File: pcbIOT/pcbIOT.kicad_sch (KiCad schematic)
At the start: 30 parts, among them IC1 NRF52832-QFAA-G-R7, IC2 TPS62841DGRR, J1 Battery power in, J2 Conn_01x08_Socket, J3 Conn_01x03_Pin, J4 Conn_01x06_Socket, J5 Conn_01x06_Socket, X1 32MHz

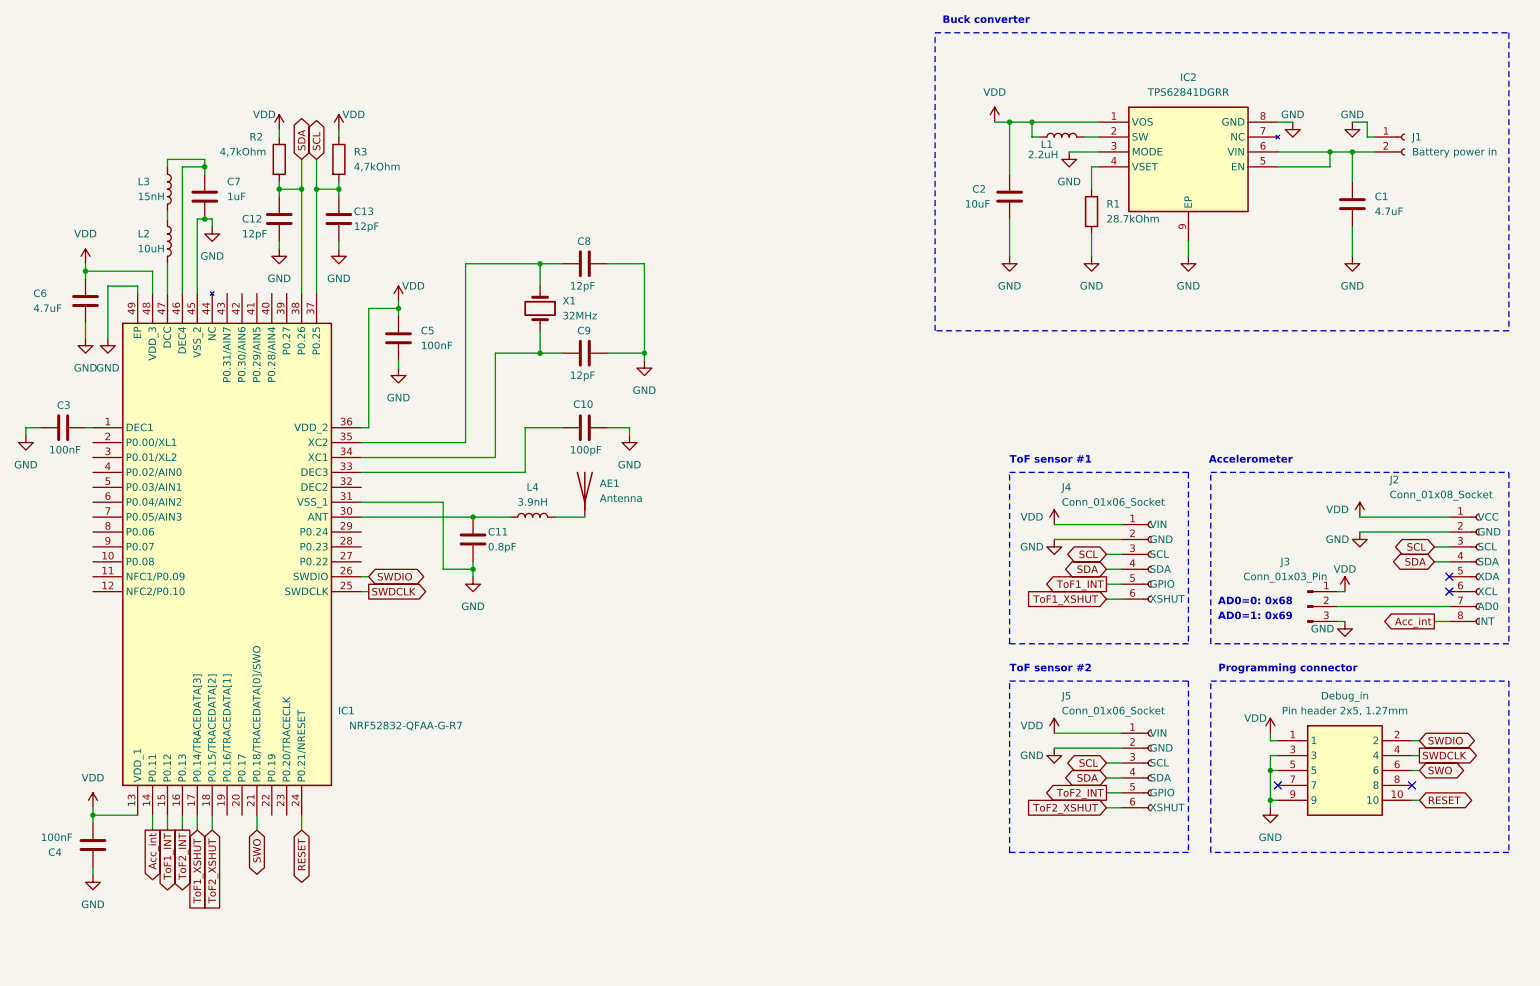
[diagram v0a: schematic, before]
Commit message: Update pcbIOT.kicad_sch
Vervangen buck converter en aanpassing weerstandswaarde naar correcte value
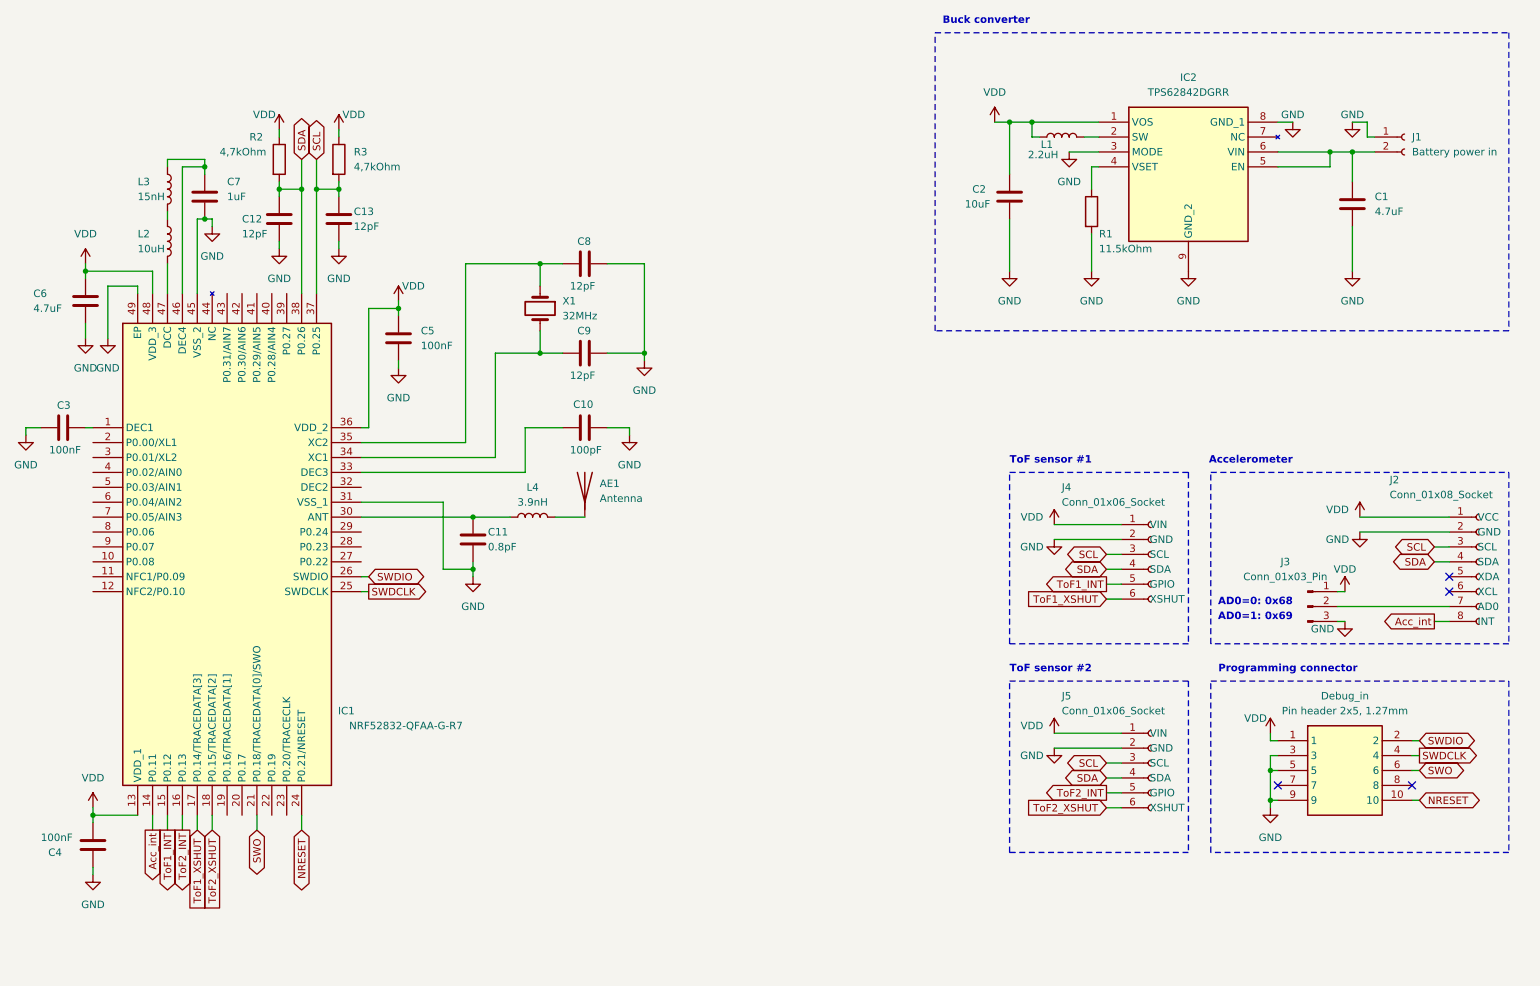
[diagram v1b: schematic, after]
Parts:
- removed IC2: TPS62841DGRR, SOP65P490X110-9N, symbol TPS62841DGRR:TPS62841DGRR
- added IC2: TPS62842DGRR, SOP65P490X110-9N, symbol TPS62842DGRR:TPS62842DGRR
- R1: value 28.7kOhm -> 11.5kOhm
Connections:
- net GND: now also IC2.3 (MODE), IC2.8 (GND_1), IC2.9 (GND_2)
- net VDD: now also IC2.1 (VOS)
- net at L1.2: now also IC2.2 (SW)
- net at R1.1: now also IC2.4 (VSET)
- net at C1.1, J1.2 (Pin_2): now also IC2.5 (EN), IC2.6 (VIN)
- net RESET renamed NRESET

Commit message: Update pcbIOT.kicad_sch
Laatste versie schema + alle footprints ok
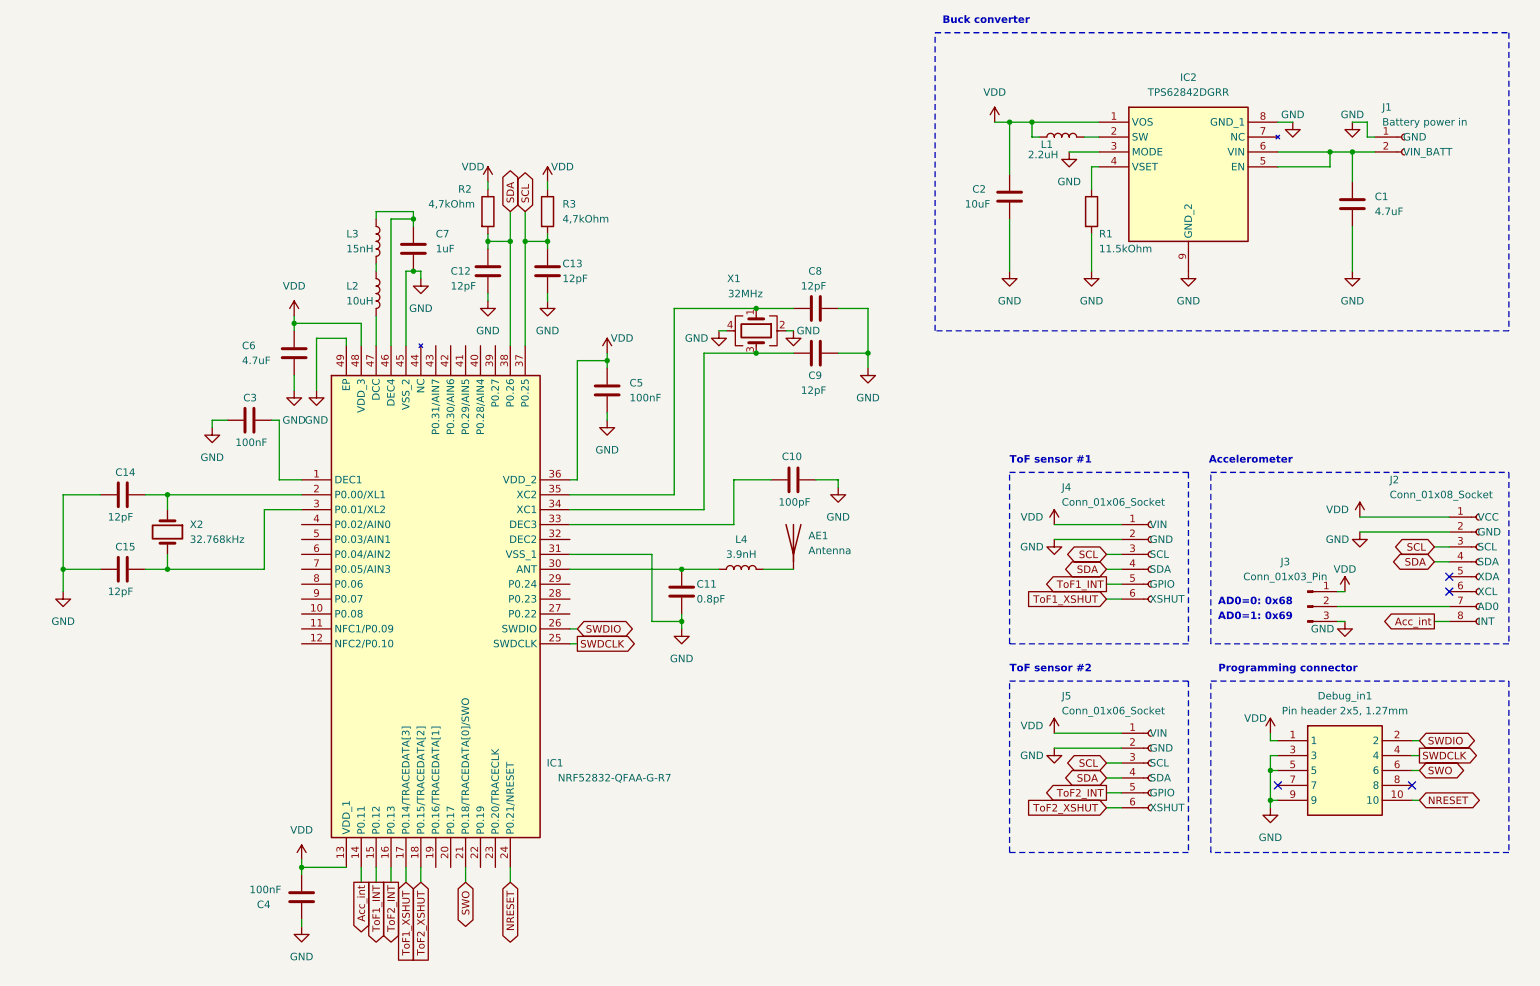
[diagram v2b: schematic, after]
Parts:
- removed X1: 32MHz, symbol Device:Crystal
- added C14, C15: 12pF, Capacitor_SMD:C_0603_1608Metric, symbol Device:C
- added X1: 32MHz, footprints:CX2016DB32000D0FLJCC, symbol Device:Crystal_GND24
- added X2: 32.768kHz, footprints:NX3215SA32768KSTDMUA9, symbol Device:Crystal
- AE1: footprint (none) -> RF_Antenna:Texas_SWRA117D_2.4GHz_Right
- C1, C10, C11, C12, C13, C2, C3, C4, C5, C6, C7, C8, C9: footprint (none) -> Capacitor_SMD:C_0603_1608Metric
- Debug_in1: renamed from Debug_in; footprint FTSH10501LDVK -> footprints:FTSH10501LDVK
- IC1: footprint QFN40P600X600X95-49N -> footprints:QFN40P600X600X95-49N
- IC2: footprint SOP65P490X110-9N -> footprints:SOP65P490X110-9N
- J1: footprint (none) -> Connector_JST:JST_PH_B2B-PH-K_1x02_P2.00mm_Vertical
- J2: footprint (none) -> Connector_PinSocket_2.54mm:PinSocket_1x08_P2.54mm_Vertical
- J3: footprint (none) -> Connector_PinHeader_2.54mm:PinHeader_1x03_P2.54mm_Vertical
- J4, J5: footprint (none) -> Connector_PinSocket_2.54mm:PinSocket_1x06_P2.54mm_Vertical
- L1: footprint (none) -> Inductor_SMD:L_Murata_DFE201610P
- L2: footprint (none) -> Inductor_SMD:L_0603_1608Metric_Pad1.05x0.95mm_HandSolder
- L3: footprint (none) -> footprints:LQW18AS10NG0CD
- L4: footprint (none) -> Inductor_SMD:L_01005_0402Metric_Pad0.57x0.30mm_HandSolder
- R1, R2, R3: footprint (none) -> Resistor_SMD:R_0603_1608Metric
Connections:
- net GND: now also C14.2, C15.2, X1.2, X1.4
- net at C8.2, IC1.35 (XC2): now also X1.1
- net at C9.2, IC1.34 (XC1): now also X1.3
- net at IC1.2 (P0.00/XL1): now also C14.1, X2.1
- net at IC1.3 (P0.01/XL2): now also C15.1, X2.2
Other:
- moved on the sheet: AE1, C10, C11, C12, C13, C3, C4, C5, C6, C7, C8, C9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

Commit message: pcb bijna af
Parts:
- added R4: 1.5kOhm, Resistor_SMD:R_0805_2012Metric_Pad1.20x1.40mm_HandSolder, symbol Device:R
- C1, C10, C11, C12, C13, C14, C15, C2, C3, C4, C5, C6, C7, C8, C9: footprint Capacitor_SMD:C_0603_1608Metric -> Capacitor_SMD:C_0805_2012Metric_Pad1.18x1.45mm_HandSolder
- L4: footprint Inductor_SMD:L_01005_0402Metric_Pad0.57x0.30mm_HandSolder -> Inductor_SMD:L_0805_2012Metric_Pad1.15x1.40mm_HandSolder
- R1: value 11.5kOhm -> 10kOhm; footprint Resistor_SMD:R_0603_1608Metric -> Resistor_SMD:R_0805_2012Metric_Pad1.20x1.40mm_HandSolder
- R2, R3: footprint Resistor_SMD:R_0603_1608Metric -> Resistor_SMD:R_0805_2012Metric_Pad1.20x1.40mm_HandSolder
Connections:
- net GND: now also R4.2; no longer R1.2
- new net: R1.2, R4.1
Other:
- moved on the sheet: R1
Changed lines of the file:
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@@
-    (stroke (width 0) (type default))
-  )
-  (wire (pts (xy 209.55 52.07) (xy 209.55 58.42))
     (stroke (width 0) (type default))
   )
@@
     (stroke (width 0) (type default))
   )
-  (wire (pts (xy 209.55 40.64) (xy 209.55 44.45))
-    (stroke (width 0) (type default))
-  )
   (wire (pts (xy 95.25 58.42) (xy 93.98 58.42))
     (stroke (width 0) (type default))
@@
     (stroke (width 0) (type default))
   )
+  (wire (pts (xy 209.55 49.53) (xy 209.55 50.8))
+    (stroke (width 0) (type default))
+  )
   (wire (pts (xy 212.09 149.86) (xy 214.63 149.86))
     (stroke (width 0) (type default))
@@
   )
   (wire (pts (xy 71.12 93.98) (xy 71.12 83.82))
+    (stroke (width 0) (type default))
+  )
+  (wire (pts (xy 209.55 40.64) (xy 209.55 41.91))
     (stroke (width 0) (type default))
   )
@@
       (effects (font (size 1.27 1.27)) (justify left))
     )
-    (property "Footprint" "Capacitor_SMD:C_0603_1608Metric" (at 74.6252 76.2 0)
+    (property "Footprint" "Capacitor_SMD:C_0805_2012Metric_Pad1.18x1.45mm_HandSolder" (at 74.6252 76.2 0)
       (effects (font (size 1.27 1.27)) hide)
     )
@@
       (effects (font (size 1.27 1.27)) (justify left))
     )
-    (property "Footprint" "Capacitor_SMD:C_0603_1608Metric" (at 158.75 65.7352 0)
+    (property "Footprint" "Capacitor_SMD:C_0805_2012Metric_Pad1.18x1.45mm_HandSolder" (at 158.75 65.7352 0)
       (effects (font (size 1.27 1.27)) hide)
     )
@@
       (effects (font (size 1.27 1.27)) (justify left))
     )
-    (property "Footprint" "Capacitor_SMD:C_0603_1608Metric" (at 40.64 110.1852 0)
+    (property "Footprint" "Capacitor_SMD:C_0805_2012Metric_Pad1.18x1.45mm_HandSolder" (at 40.64 110.1852 0)
       (effects (font (size 1.27 1.27)) hide)
     )
@@
       (effects (font (size 1.27 1.27)) (justify left))
     )
-    (property "Footprint" "Capacitor_SMD:C_0603_1608Metric" (at 158.75 73.3552 0)
+    (property "Footprint" "Capacitor_SMD:C_0805_2012Metric_Pad1.18x1.45mm_HandSolder" (at 158.75 73.3552 0)
       (effects (font (size 1.27 1.27)) hide)
     )
@@
       (effects (font (size 1.27 1.27)) (justify left))
     )
-    (property "Footprint" "Capacitor_SMD:C_0603_1608Metric" (at 40.64 97.4852 0)
+    (property "Footprint" "Capacitor_SMD:C_0805_2012Metric_Pad1.18x1.45mm_HandSolder" (at 40.64 97.4852 0)
       (effects (font (size 1.27 1.27)) hide)
     )
@@
       (effects (font (size 1.27 1.27)) (justify left))
     )
-    (property "Footprint" "Resistor_SMD:R_0603_1608Metric" (at 115.062 48.26 90)
+    (property "Footprint" "Resistor_SMD:R_0805_2012Metric_Pad1.20x1.40mm_HandSolder" (at 115.062 48.26 90)
       (effects (font (size 1.27 1.27)) hide)
     )
@@
       (effects (font (size 1.27 1.27)) (justify left))
     )
-    (property "Footprint" "Capacitor_SMD:C_0603_1608Metric" (at 117.8052 62.23 0)
+    (property "Footprint" "Capacitor_SMD:C_0805_2012Metric_Pad1.18x1.45mm_HandSolder" (at 117.8052 62.23 0)
       (effects (font (size 1.27 1.27)) hide)
     )
@@
       (effects (font (size 1.27 1.27)))
     )
-    (property "Footprint" "Inductor_SMD:L_01005_0402Metric_Pad0.57x0.30mm_HandSolder" (at 149.86 109.22 0)
+    (property "Footprint" "Inductor_SMD:L_0805_2012Metric_Pad1.15x1.40mm_HandSolder" (at 149.86 109.22 0)
       (effects (font (size 1.27 1.27)) hide)
     )
@@
       (effects (font (size 1.27 1.27)) (justify left))
     )
-    (property "Footprint" "Capacitor_SMD:C_0603_1608Metric" (at 69.85 82.8548 0)
+    (property "Footprint" "Capacitor_SMD:C_0805_2012Metric_Pad1.18x1.45mm_HandSolder" (at 69.85 82.8548 0)
       (effects (font (size 1.27 1.27)) hide)
     )
@@
       (effects (font (size 1.27 1.27)) (justify left))
     )
-    (property "Footprint" "Capacitor_SMD:C_0603_1608Metric" (at 107.6452 62.23 0)
+    (property "Footprint" "Capacitor_SMD:C_0805_2012Metric_Pad1.18x1.45mm_HandSolder" (at 107.6452 62.23 0)
       (effects (font (size 1.27 1.27)) hide)
     )
@@
       (effects (font (size 1.27 1.27)) (justify left))
     )
-    (property "Footprint" "Capacitor_SMD:C_0603_1608Metric" (at 196.5452 49.53 0)
+    (property "Footprint" "Capacitor_SMD:C_0805_2012Metric_Pad1.18x1.45mm_HandSolder" (at 196.5452 49.53 0)
       (effects (font (size 1.27 1.27)) hide)
     )
@@
       (effects (font (size 1.27 1.27)) (justify left))
     )
-    (property "Footprint" "Capacitor_SMD:C_0603_1608Metric" (at 127.9652 82.55 0)
+    (property "Footprint" "Capacitor_SMD:C_0805_2012Metric_Pad1.18x1.45mm_HandSolder" (at 127.9652 82.55 0)
       (effects (font (size 1.27 1.27)) hide)
     )
@@
       (effects (font (size 1.27 1.27)) (justify left))
     )
-    (property "Footprint" "Capacitor_SMD:C_0603_1608Metric" (at 254.9652 50.8 0)
+    (property "Footprint" "Capacitor_SMD:C_0805_2012Metric_Pad1.18x1.45mm_HandSolder" (at 254.9652 50.8 0)
       (effects (font (size 1.27 1.27)) hide)
     )
@@
       (effects (font (size 1.27 1.27)) (justify left))
     )
-    (property "Footprint" "Capacitor_SMD:C_0603_1608Metric" (at 75.8952 168.91 0)
+    (property "Footprint" "Capacitor_SMD:C_0805_2012Metric_Pad1.18x1.45mm_HandSolder" (at 75.8952 168.91 0)
       (effects (font (size 1.27 1.27)) hide)
     )
@@
       (effects (font (size 1.27 1.27)) (justify left))
     )
-    (property "Footprint" "Capacitor_SMD:C_0603_1608Metric" (at 140.6652 116.84 0)
+    (property "Footprint" "Capacitor_SMD:C_0805_2012Metric_Pad1.18x1.45mm_HandSolder" (at 140.6652 116.84 0)
       (effects (font (size 1.27 1.27)) hide)
     )
@@
     )
   )
-  (symbol (lib_id "Device:R") (at 209.55 48.26 0) (unit 1)
-    (in_bom yes) (on_board yes) (dnp no)
-    (property "Reference" "R1" (at 210.82 52.07 0)
-      (effects (font (size 1.27 1.27)) (justify left))
-    )
-    (property "Value" "11.5kOhm" (at 210.82 54.61 0)
-      (effects (font (size 1.27 1.27)) (justify left))
-    )
-    (property "Footprint" "Resistor_SMD:R_0603_1608Metric" (at 207.772 48.26 90)
-      (effects (font (size 1.27 1.27)) hide)
-    )
-    (property "Datasheet" "~" (at 209.55 48.26 0)
+  (symbol (lib_id "Device:R") (at 209.55 45.72 0) (unit 1)
+    (in_bom yes) (on_board yes) (dnp no)
+    (property "Reference" "R1" (at 210.82 49.53 0)
+      (effects (font (size 1.27 1.27)) (justify left))
+    )
+    (property "Value" "10kOhm" (at 210.82 52.07 0)
+      (effects (font (size 1.27 1.27)) (justify left))
+    )
+    (property "Footprint" "Resistor_SMD:R_0805_2012Metric_Pad1.20x1.40mm_HandSolder" (at 207.772 45.72 90)
+      (effects (font (size 1.27 1.27)) hide)
+    )
+    (property "Datasheet" "~" (at 209.55 45.72 0)
       (effects (font (size 1.27 1.27)) hide)
     )
@@
       (effects (font (size 1.27 1.27)) (justify left))
     )
-    (property "Footprint" "Capacitor_SMD:C_0603_1608Metric" (at 94.9452 58.42 0)
+    (property "Footprint" "Capacitor_SMD:C_0805_2012Metric_Pad1.18x1.45mm_HandSolder" (at 94.9452 58.42 0)
       (effects (font (size 1.27 1.27)) hide)
     )
@@
     )
   )
+  (symbol (lib_id "Device:R") (at 209.55 54.61 0) (unit 1)
+    (in_bom yes) (on_board yes) (dnp no)
+    (property "Reference" "R4" (at 210.82 58.42 0)
+      (effects (font (size 1.27 1.27)) (justify left))
+    )
+    (property "Value" "1.5kOhm" (at 210.82 60.96 0)
+      (effects (font (size 1.27 1.27)) (justify left))
+    )
+    (property "Footprint" "Resistor_SMD:R_0805_2012Metric_Pad1.20x1.40mm_HandSolder" (at 207.772 54.61 90)
+      (effects (font (size 1.27 1.27)) hide)
+    )
+    (property "Datasheet" "~" (at 209.55 54.61 0)
+      (effects (font (size 1.27 1.27)) hide)
+    )
+    (pin "1")
+    (pin "2")
+    (instances
+      (project "pcbIOT"
+        (path "/79d26ad8-5789-46cf-878f-e49e2e4d86d0"
+          (reference "R4") (unit 1)
+        )
+      )
+    )
+  )
   (symbol (lib_id "power:GND") (at 34.29 113.03 0) (unit 1)
     (in_bom yes) (on_board yes) (dnp no) (fields_autoplaced)
@@
       (effects (font (size 1.27 1.27)) (justify left))
     )
-    (property "Footprint" "Capacitor_SMD:C_0603_1608Metric" (at 154.94 94.9452 0)
+    (property "Footprint" "Capacitor_SMD:C_0805_2012Metric_Pad1.18x1.45mm_HandSolder" (at 154.94 94.9452 0)
       (effects (font (size 1.27 1.27)) hide)
     )
@@
       (effects (font (size 1.27 1.27)) (justify left))
     )
-    (property "Footprint" "Resistor_SMD:R_0603_1608Metric" (at 104.902 48.26 90)
-      (effects (font (size 1.27 1.27)) hide)
-    )
+    (property "Footprint" "Resistor_SMD:R_0805_2012Metric_Pad1.20x1.40mm_HandSolder" (at 104.902 48.26 90)
+      (effects (font (size 1.27 1.27)) hide)
+    )
